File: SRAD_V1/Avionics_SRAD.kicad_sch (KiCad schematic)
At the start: 20 parts, among them U1 TPS563200, U10 AS5F31G04SND-08LIN, U11 MS5607-02BA, U12 MMC5983MA, U13 MCP9808_DFN, U14 KX134-1211, U16 ASM330LHH, U8 STM32F407VGTx, U9 MAX-M10S

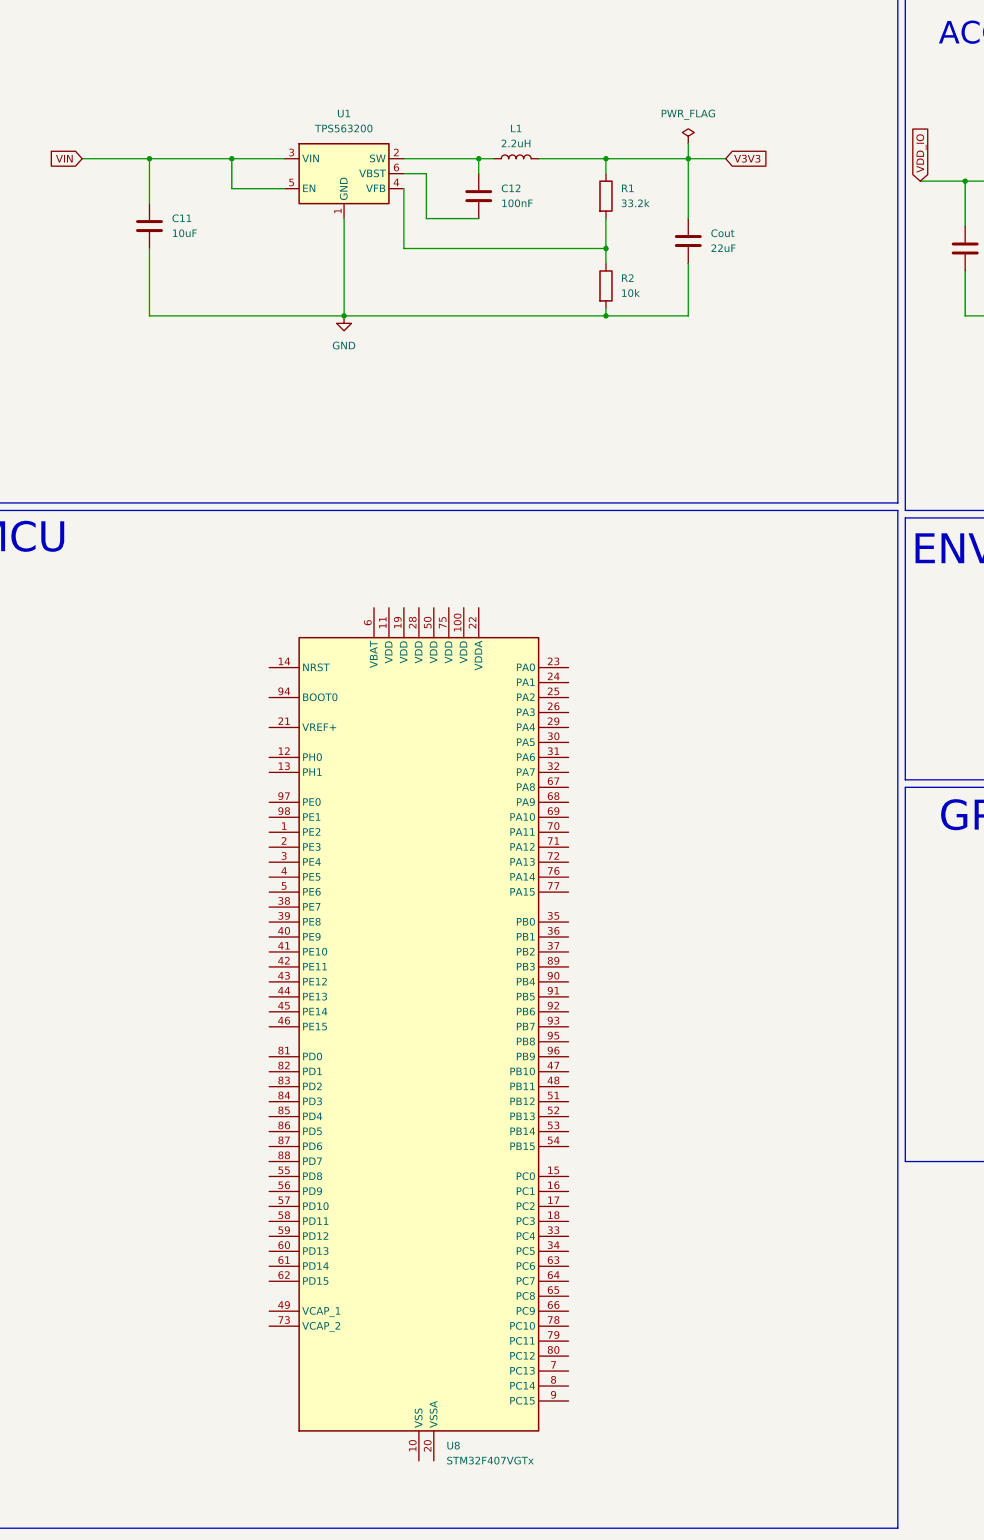
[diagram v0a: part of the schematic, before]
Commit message: added correct models and linked footprints
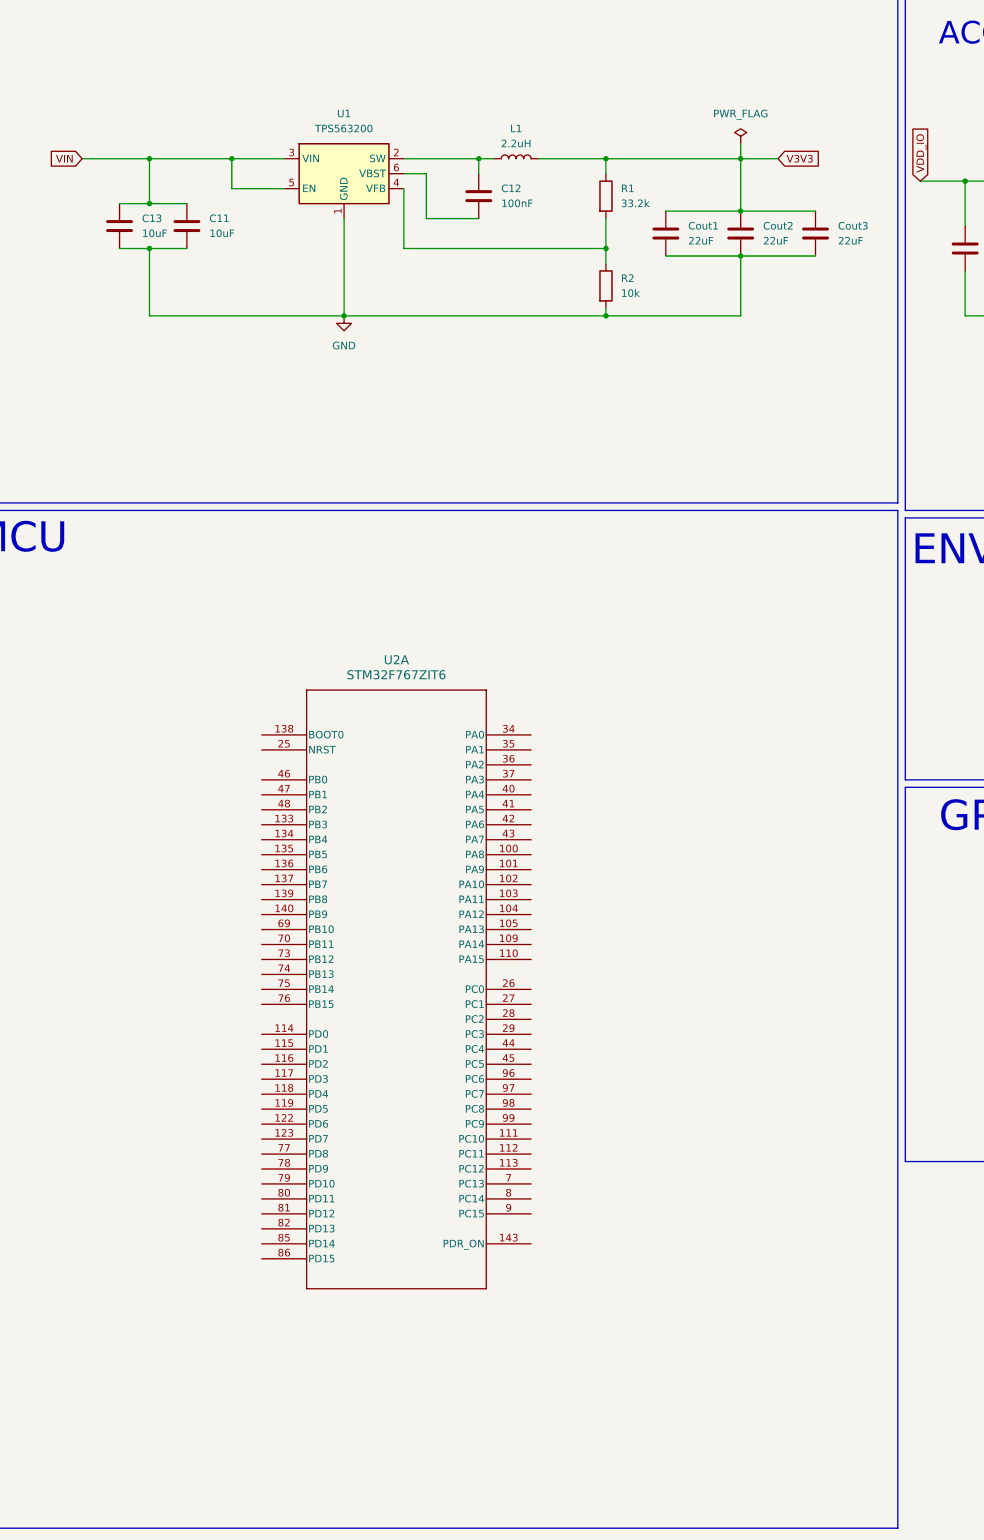
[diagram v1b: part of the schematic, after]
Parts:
- removed U8: STM32F407VGTx, Package_QFP:LQFP-100_14x14mm_P0.5mm, symbol MCU_ST_STM32F4:STM32F407VGTx
- added C13: 10uF, Capacitor_SMD:C_0805_2012Metric, symbol Device:C
- added Cout2, Cout3: 22uF, Capacitor_SMD:C_0603_1608Metric, symbol Device:C
- added U2: STM32F767ZIT6, STM32F767ZIT6:LQFP144-20x20mm_STM, symbol STM32F767ZIT6:STM32F767ZIT6
- C11, C12: footprint (none) -> Capacitor_SMD:C_0805_2012Metric
- Cout1: renamed from Cout; footprint (none) -> Capacitor_SMD:C_0603_1608Metric
- L1: footprint (none) -> VLS6045EX-2R2N:IND_VLS6045EX-2R2N
- R1: footprint Resistor_SMD:R_0603_1608Metric -> Resistor_SMD:R_0402_1005Metric
- U10: footprint footprints:SON127P600X800X80-8N -> AS5F31G04SND-08LIN:SON127P600X800X80-8N
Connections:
- net GND: now also C13.2, Cout2.2, Cout3.2
- net V3V3: now also Cout2.1, Cout3.1
- net VIN: now also C13.1
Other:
- moved on the sheet: C11, Cout1

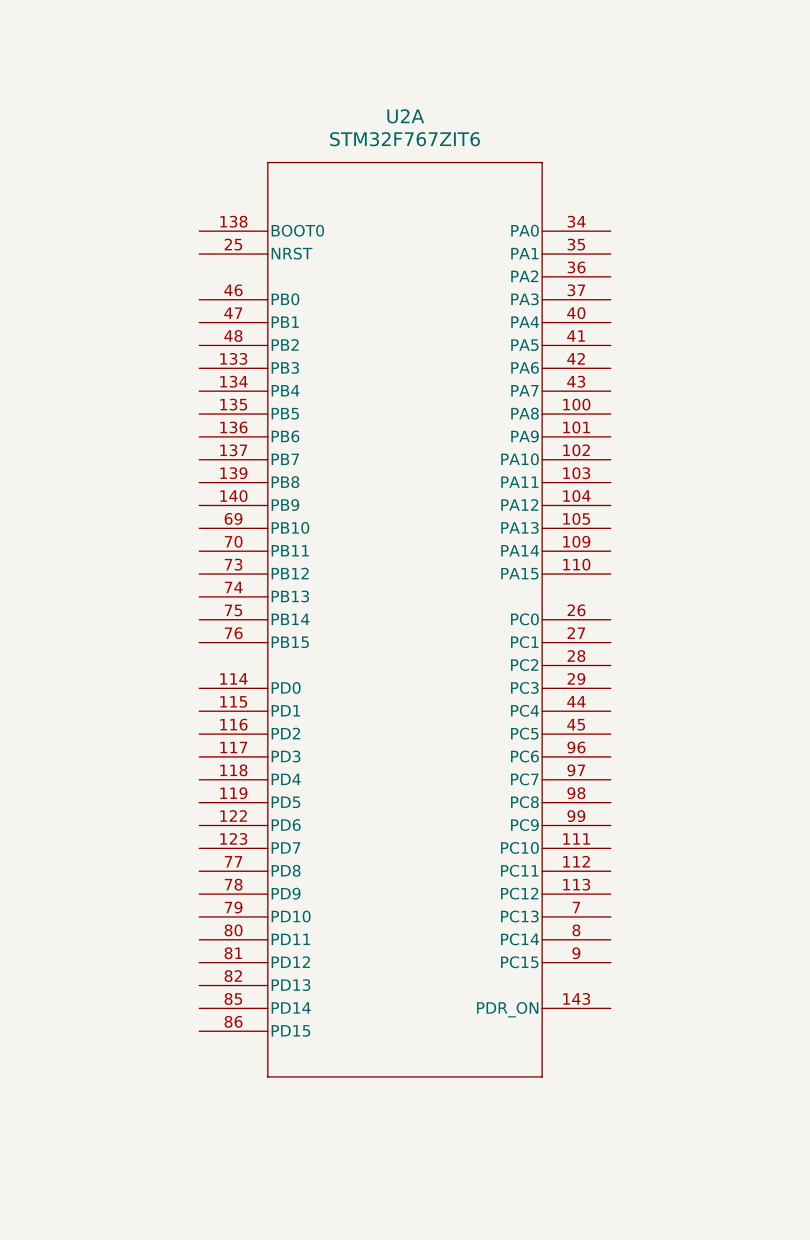
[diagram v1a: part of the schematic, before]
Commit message: Changing file structure for merging in future
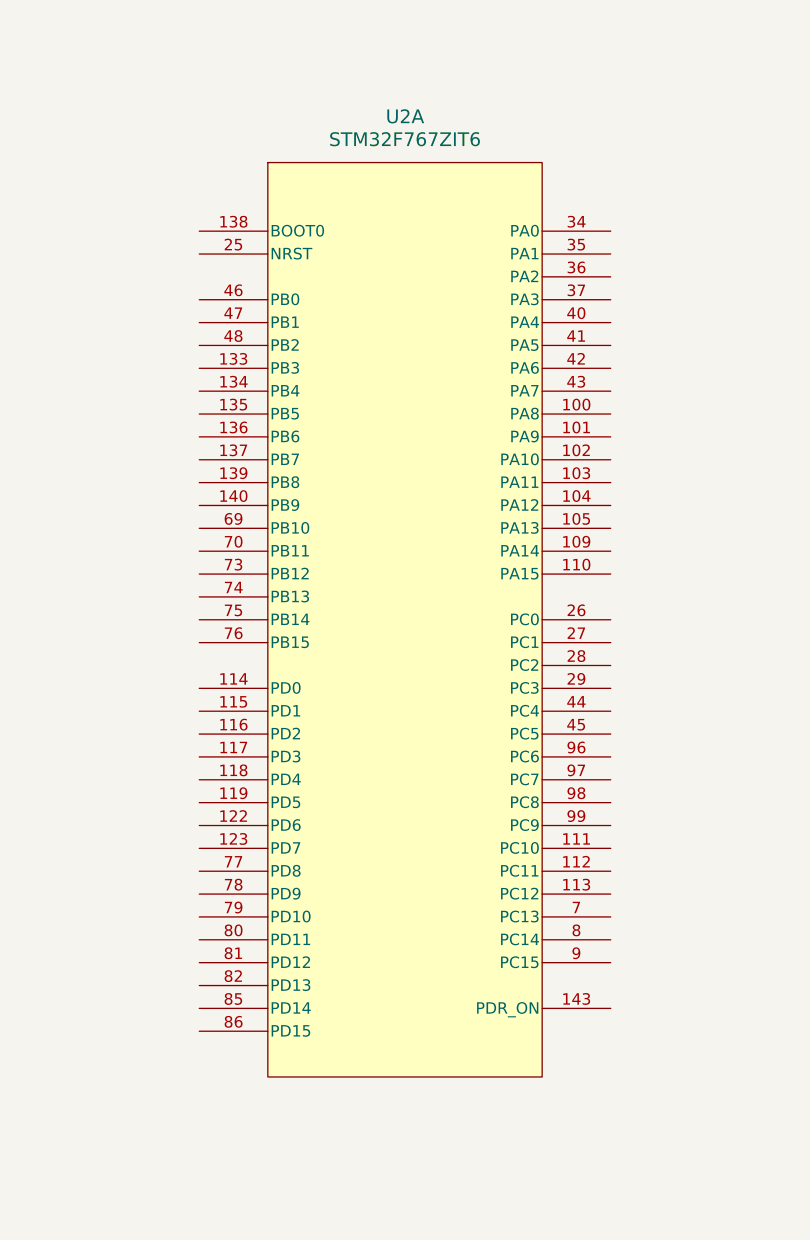
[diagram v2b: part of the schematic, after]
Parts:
- U2: footprint STM32F767ZIT6:LQFP144-20x20mm_STM -> LQFP144-20x20mm_STM
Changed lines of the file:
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@@
 			)
 		)
-		(property "Footprint" "STM32F767ZIT6:LQFP144-20x20mm_STM"
+		(property "Footprint" "LQFP144-20x20mm_STM"
 			(at 63.5 148.59 0)
 			(effects
